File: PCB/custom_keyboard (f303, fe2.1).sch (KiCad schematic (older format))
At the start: 425 parts, among them IC1 FE2.1, J2 Conn_01x03_Male, J5 AVR-ISP-6, Q1 DTC123J, SW1 SW_Push, U1 24LC02BT-I/SN, U10 PRTR5V0U2X, U11 XC6206P332MR, U12 74LVC1G34, U13 XC6206P332MR, U2 PRTR5V0U2X, U3 PRTR5V0U2X, U4 PRTR5V0U2X, U5 PRTR5V0U2X, U6 PRTR5V0U2X, U7 PRTR5V0U2X, U8 PRTR5V0U2X, U9 STM32F303CBT6, Y1 8MHz, Y2 32.768KHz, Y3 12MHz

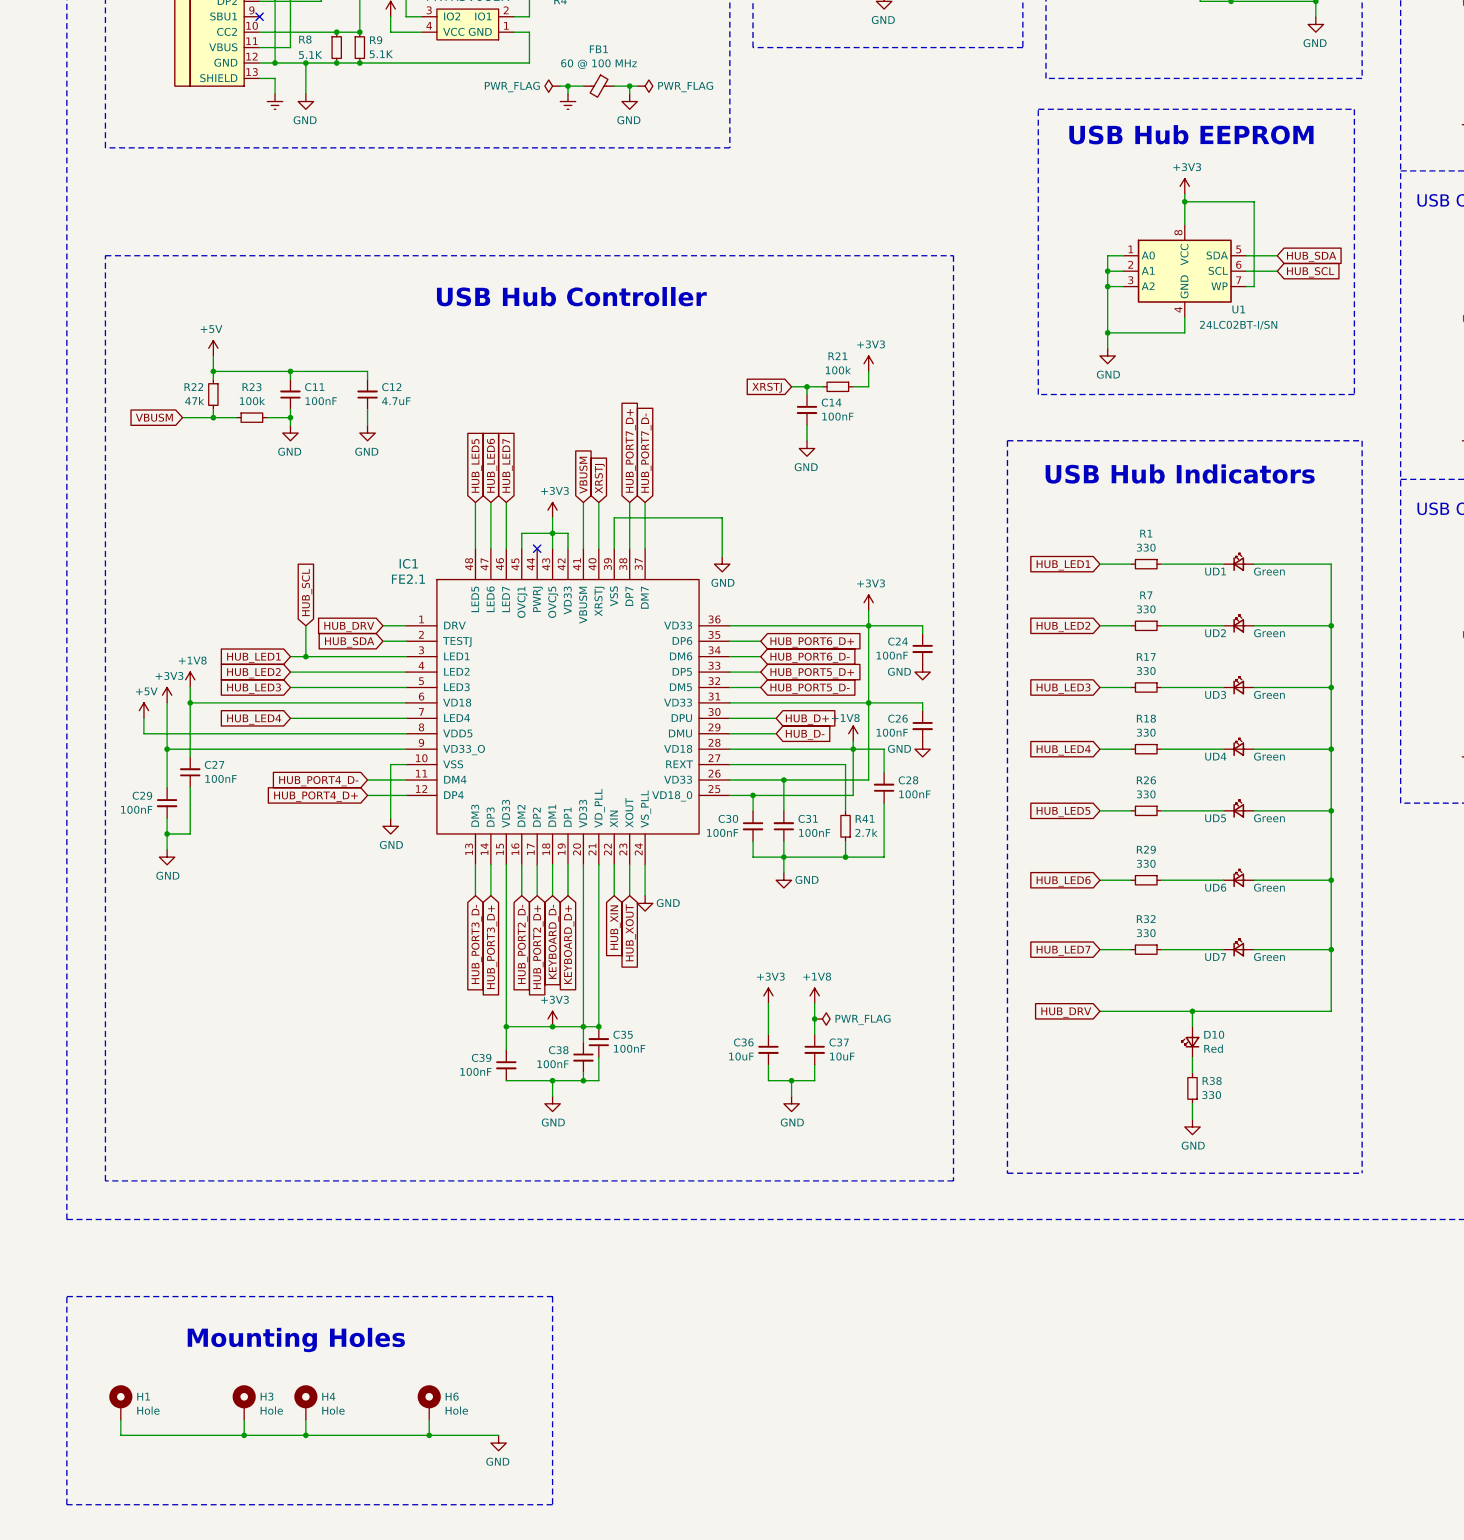
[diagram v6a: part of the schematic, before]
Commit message: Added pullups to EEPROM
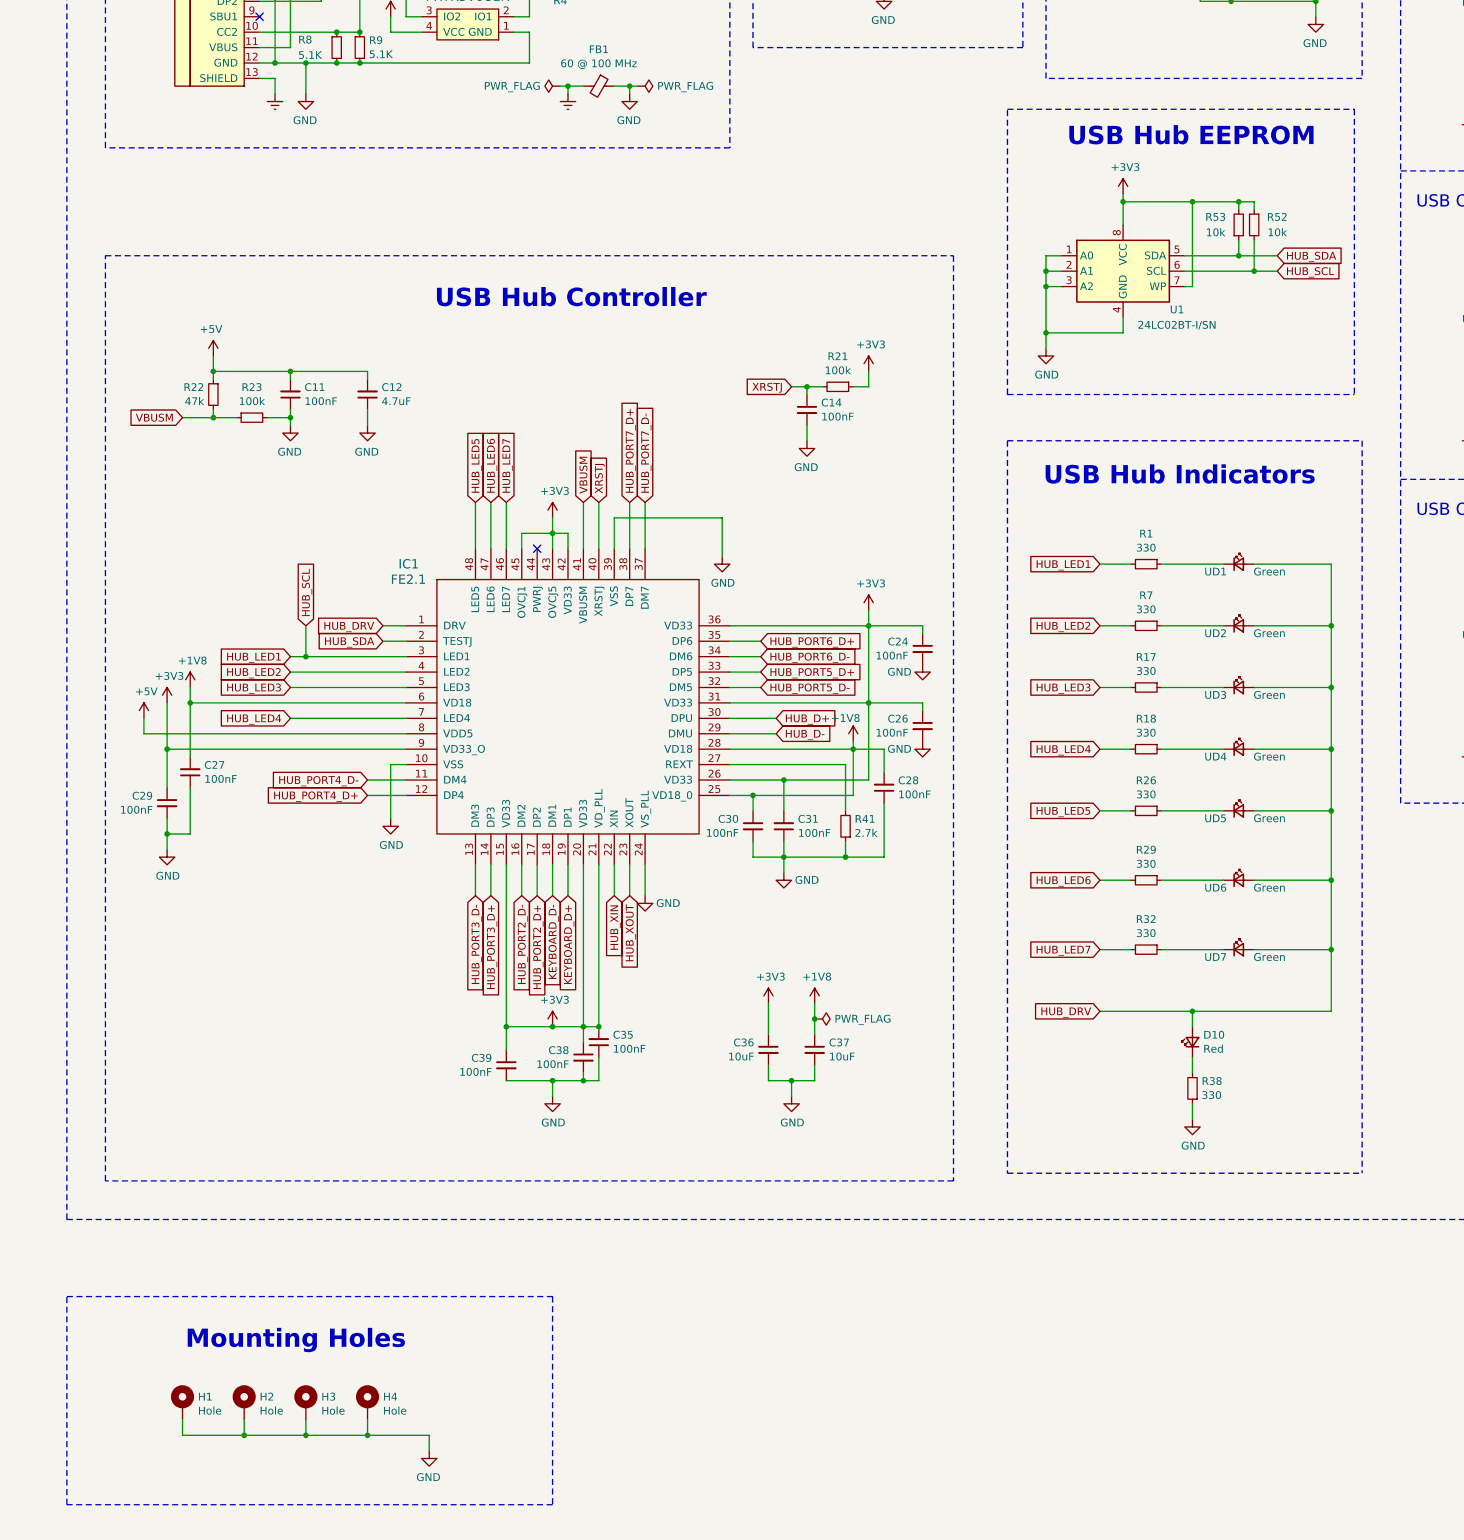
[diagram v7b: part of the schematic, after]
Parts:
- added R52, R53: 10k, Resistor_SMD:R_0805_2012Metric, symbol Device:R_Small
- R50, R51: footprint Resistor_SMD:R_0603_1608Metric -> Resistor_SMD:R_0805_2012Metric
- renumbered H3 to H2, H4 to H3, H6 to H4
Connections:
- net +3V3: now also R52.1, R53.2
- net HUB_LED1: now also R52.2
- net HUB_SDA: now also R53.1
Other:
- moved on the sheet: H1, H4, U1
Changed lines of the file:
@@
 L Memory_EEPROM:24LC02 U1
 U 1 1 AE6F59FC
-P 19850 13900
-F 0 "U1" H 20200 13650 50  0000 C CNN
-F 1 "24LC02BT-I/SN" H 20200 13550 50  0000 C CNN
-F 2 "custom-footprints:24LC04" H 19850 13900 50  0001 C CNN
-F 3 "http://ww1.microchip.com/downloads/en/DeviceDoc/21709c.pdf" H 19850 13900 50  0001 C CNN
-	1    19850 13900
+P 19450 13900
+F 0 "U1" H 19800 13650 50  0000 C CNN
+F 1 "24LC02BT-I/SN" H 19800 13550 50  0000 C CNN
+F 2 "custom-footprints:24LC04" H 19450 13900 50  0001 C CNN
+F 3 "http://ww1.microchip.com/downloads/en/DeviceDoc/21709c.pdf" H 19450 13900 50  0001 C CNN
+	1    19450 13900
 	1    0    0    -1
 $EndComp
@@
 L power:GND #PWR0100
 U 1 1 AE6F9E47
-P 19350 14400
-F 0 "#PWR0100" H 19350 14150 50  0001 C CNN
-F 1 "GND" H 19355 14227 50  0000 C CNN
-F 2 "" H 19350 14400 50  0001 C CNN
-F 3 "" H 19350 14400 50  0001 C CNN
-	1    19350 14400
+P 18950 14400
+F 0 "#PWR0100" H 18950 14150 50  0001 C CNN
+F 1 "GND" H 18955 14227 50  0000 C CNN
+F 2 "" H 18950 14400 50  0001 C CNN
+F 3 "" H 18950 14400 50  0001 C CNN
+	1    18950 14400
 	1    0    0    -1
 $EndComp
 Wire Wire Line
-	19350 14400 19350 14300
+	18950 14400 18950 14300
 Wire Wire Line
-	19350 14300 19850 14300
+	18950 14300 19450 14300
 Wire Wire Line
-	19850 14300 19850 14200
+	19450 14300 19450 14200
 Wire Wire Line
-	19350 14300 19350 14000
+	18950 14300 18950 14000
 Wire Wire Line
-	19350 13800 19450 13800
-Connection ~ 19350 14300
+	18950 13800 19050 13800
+Connection ~ 18950 14300
 Wire Wire Line
-	19450 13900 19350 13900
-Connection ~ 19350 13900
+	19050 13900 18950 13900
+Connection ~ 18950 13900
 Wire Wire Line
-	19350 13900 19350 13800
+	18950 13900 18950 13800
 Wire Wire Line
-	19450 14000 19350 14000
-Connection ~ 19350 14000
+	19050 14000 18950 14000
+Connection ~ 18950 14000
 Wire Wire Line
-	19350 14000 19350 13900
+	18950 14000 18950 13900
 Text GLabel 20450 13900 2    50   Input ~ 0
 HUB_SCL
 Text GLabel 20450 13800 2    50   Input ~ 0
 HUB_SDA
-Wire Wire Line
-	20250 13800 20450 13800
-Wire Wire Line
-	20450 13900 20250 13900
 Text GLabel 16150 17950 3    50   Input ~ 0
 HUB_XIN
@@
 L power:+3V3 #PWR095
 U 1 1 BFCEA814
-P 19850 13400
-F 0 "#PWR095" H 19850 13250 50  0001 C CNN
-F 1 "+3V3" H 19865 13573 50  0000 C CNN
-F 2 "" H 19850 13400 50  0001 C CNN
-F 3 "" H 19850 13400 50  0001 C CNN
-	1    19850 13400
+P 19450 13400
+F 0 "#PWR095" H 19450 13250 50  0001 C CNN
+F 1 "+3V3" H 19465 13573 50  0000 C CNN
+F 2 "" H 19450 13400 50  0001 C CNN
+F 3 "" H 19450 13400 50  0001 C CNN
+	1    19450 13400
 	1    0    0    -1
 $EndComp
 Wire Wire Line
-	19850 13400 19850 13450
+	19450 13400 19450 13450
 Wire Wire Line
-	20250 14000 20300 14000
+	19850 14000 19900 14000
 Wire Wire Line
-	20300 14000 20300 13450
+	19900 14000 19900 13450
 Wire Wire Line
-	20300 13450 19850 13450
-Connection ~ 19850 13450
+	19900 13450 19450 13450
+Connection ~ 19450 13450
 Wire Wire Line
-	19850 13450 19850 13600
+	19450 13450 19450 13600
 Text GLabel 19300 15800 0    50   Input ~ 0
 HUB_LED1
@@
 	20950 12850 20950 14700
 Wire Notes Line
-	20950 14700 18900 14700
-Wire Notes Line
-	18900 12850 20950 12850
-Wire Notes Line
 	18350 13800 18350 19800
 Wire Notes Line
@@
 Wire Wire Line
 	14150 12550 14350 12550
-Wire Notes Line
-	18900 14700 18900 12850
 Connection ~ 23050 16050
 Wire Wire Line
@@
 $EndComp
 $Comp
-L Mechanical:MountingHole_Pad H4
+L Mechanical:MountingHole_Pad H3
 U 1 1 6FB1B5C9
 P 14150 21250
-F 0 "H4" H 14250 21299 50  0000 L CNN
+F 0 "H3" H 14250 21299 50  0000 L CNN
 F 1 "Hole" H 14250 21208 50  0000 L CNN
 F 2 "MountingHole:MountingHole_3.2mm_M3_Pad" H 14150 21250 50  0001 C CNN
@@
 $EndComp
 $Comp
-L Mechanical:MountingHole_Pad H6
+L Mechanical:MountingHole_Pad H4
 U 1 1 6FB1CEC9
-P 14950 21250
-F 0 "H6" H 15050 21299 50  0000 L CNN
-F 1 "Hole" H 15050 21208 50  0000 L CNN
-F 2 "MountingHole:MountingHole_3.2mm_M3_Pad" H 14950 21250 50  0001 C CNN
-F 3 "~" H 14950 21250 50  0001 C CNN
-	1    14950 21250
+P 14550 21250
+F 0 "H4" H 14650 21299 50  0000 L CNN
+F 1 "Hole" H 14650 21208 50  0000 L CNN
+F 2 "MountingHole:MountingHole_3.2mm_M3_Pad" H 14550 21250 50  0001 C CNN
+F 3 "~" H 14550 21250 50  0001 C CNN
+	1    14550 21250
 	1    0    0    -1
 $EndComp
@@
 L power:GND #PWR0283
 U 1 1 7017E3FA
-P 15400 21450
-F 0 "#PWR0283" H 15400 21200 50  0001 C CNN
-F 1 "GND" H 15405 21277 50  0000 C CNN
-F 2 "" H 15400 21450 50  0001 C CNN
-F 3 "" H 15400 21450 50  0001 C CNN
-	1    15400 21450
+P 14950 21550
+F 0 "#PWR0283" H 14950 21300 50  0001 C CNN
+F 1 "GND" H 14955 21377 50  0000 C CNN
+F 2 "" H 14950 21550 50  0001 C CNN
+F 3 "" H 14950 21550 50  0001 C CNN
+	1    14950 21550
 	-1   0    0    -1
 $EndComp
 Wire Wire Line
-	15400 21450 14950 21450
-Wire Wire Line
 	14150 21450 14150 21350
 Wire Wire Line
-	14950 21350 14950 21450
+	14550 21350 14550 21450
 $Comp
 L Mechanical:MountingHole_Pad H1
 U 1 1 72E52B19
-P 12950 21250
-F 0 "H1" H 13050 21299 50  0000 L CNN
-F 1 "Hole" H 13050 21208 50  0000 L CNN
-F 2 "MountingHole:MountingHole_3.2mm_M3_Pad" H 12950 21250 50  0001 C CNN
-F 3 "~" H 12950 21250 50  0001 C CNN
-	1    12950 21250
+P 13350 21250
+F 0 "H1" H 13450 21299 50  0000 L CNN
+F 1 "Hole" H 13450 21208 50  0000 L CNN
+F 2 "MountingHole:MountingHole_3.2mm_M3_Pad" H 13350 21250 50  0001 C CNN
+F 3 "~" H 13350 21250 50  0001 C CNN
+	1    13350 21250
 	1    0    0    -1
 $EndComp
 $Comp
-L Mechanical:MountingHole_Pad H3
+L Mechanical:MountingHole_Pad H2
 U 1 1 72E561B5
 P 13750 21250
-F 0 "H3" H 13850 21299 50  0000 L CNN
+F 0 "H2" H 13850 21299 50  0000 L CNN
 F 1 "Hole" H 13850 21208 50  0000 L CNN
 F 2 "MountingHole:MountingHole_3.2mm_M3_Pad" H 13750 21250 50  0001 C CNN
@@
 $EndComp
 Wire Wire Line
-	12950 21450 12950 21350
+	13350 21450 13350 21350
 Wire Wire Line
 	13750 21350 13750 21450
-Connection ~ 14950 21450
 Connection ~ 13750 21450
 Wire Wire Line
@@
 KEYBOARD_D+
 Wire Wire Line
-	12950 21450 13750 21450
-Wire Wire Line
-	14150 21450 14950 21450
+	14150 21450 14550 21450
 $Comp
 L power:+5V #PWR0158
@@
 F 0 "R51" V 9700 20500 50  0000 C CNN
 F 1 "10k" V 9600 20500 50  0000 C CNN
-F 2 "Resistor_SMD:R_0603_1608Metric" H 9800 20500 50  0001 C CNN
+F 2 "Resistor_SMD:R_0805_2012Metric" H 9800 20500 50  0001 C CNN
 F 3 "~" H 9800 20500 50  0001 C CNN
 	1    9800 20500
@@
 F 0 "R50" V 9600 20350 50  0000 C CNN
 F 1 "10k" V 9700 20350 50  0000 C CNN
-F 2 "Resistor_SMD:R_0603_1608Metric" H 9800 20350 50  0001 C CNN
+F 2 "Resistor_SMD:R_0805_2012Metric" H 9800 20350 50  0001 C CNN
 F 3 "~" H 9800 20350 50  0001 C CNN
 	1    9800 20350
 	0    -1   1    0
 $EndComp
+$Comp
+L Device:R_Small R53
+U 1 1 61D98DD0
+P 20200 13600
+F 0 "R53" H 20050 13550 50  0000 C CNN
+F 1 "10k" H 20050 13650 50  0000 C CNN
+F 2 "Resistor_SMD:R_0805_2012Metric" H 20200 13600 50  0001 C CNN
+F 3 "~" H 20200 13600 50  0001 C CNN
+	1    20200 13600
+	1    0    0    1
+$EndComp
+Wire Notes Line
+	18700 14700 18700 12850
+Wire Notes Line
+	18700 12850 20950 12850
+Wire Notes Line
+	18700 14700 20950 14700
+Wire Wire Line
+	13350 21450 13750 21450
+Wire Wire Line
+	14550 21450 14950 21450
+Wire Wire Line
+	14950 21450 14950 21550
+Connection ~ 14550 21450
+Wire Wire Line
+	19850 13800 20200 13800
+Connection ~ 20200 13800
+Wire Wire Line
+	20200 13800 20450 13800
+Wire Wire Line
+	19850 13900 20300 13900
+Connection ~ 20300 13900
+Wire Wire Line
+	20300 13900 20450 13900
+Wire Wire Line
+	20200 13700 20200 13800
+Wire Wire Line
+	20300 13700 20300 13900
+$Comp
+L Device:R_Small R52
+U 1 1 61D9C5AC
+P 20300 13600
+F 0 "R52" H 20150 13650 50  0000 C CNN
+F 1 "10k" H 20150 13550 50  0000 C CNN
+F 2 "Resistor_SMD:R_0805_2012Metric" H 20300 13600 50  0001 C CNN
+F 3 "~" H 20300 13600 50  0001 C CNN
+	1    20300 13600
+	-1   0    0    -1
+$EndComp
+Wire Wire Line
+	20300 13500 20300 13450
+Wire Wire Line
+	20300 13450 20200 13450
+Connection ~ 19900 13450
+Wire Wire Line
+	20200 13500 20200 13450
+Connection ~ 20200 13450
+Wire Wire Line
+	20200 13450 19900 13450
 $EndSCHEMATC

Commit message: Added power control to downstream ports
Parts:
- added C44, C46: 10uF, Capacitor_SMD:C_0805_2012Metric, symbol Device:C_Small
- added C45, C47: 0.1uF, Capacitor_SMD:C_0805_2012Metric, symbol Device:C_Small
- added R54, R55, R56: 100k, Resistor_SMD:R_0603_1608Metric, symbol Device:R_Small
- added TP1: HUB_D-, symbol Connector:TestPoint
- added TP2: HUB_D+, symbol Connector:TestPoint
- added TP3: INPUT_GND, symbol Connector:TestPoint
- added TP4: EXTRA_1, symbol Connector:TestPoint
- added U14, U15: MIC2505, custom-footprints:MIC2505, symbol custom:MIC2505
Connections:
- net +3V3: now also R54.1, R55.1, R56.1; no longer IC1.43 (OVCJ5), IC1.45 (OVCJ1)
- net +5V: now also C45.1, C47.1, U14.5 (IN), U14.7 (IN), U15.5 (IN), U15.7 (IN); no longer C10.1, C13.1, C2.1, C23.1, C25.1, C34.1, C40.1, F2.1, F2.2, F3.1, F3.2, F4.1, F4.2, F5.1, F5.2, F6.1, F6.2, F7.1, F7.2, U11.3 (VI), USB2.11 (VBUS), USB2.2 (VBUS), USB3.1 (VBUS), USB4.1 (VBUS), USB5.11 (VBUS), USB5.2 (VBUS), USB6.1 (VBUS), USB7.11 (VBUS), USB7.2 (VBUS)
- net EXTRA_1: now also TP4.1
- net GND: now also C44.2, C45.2, C46.2, C47.2, TP3.1, U14.3 (GND), U15.3 (GND)
- net HUB_D+: now also TP2.1
- net HUB_D-: now also TP1.1
- net KEYBOARD_SCL: now also OL1.2 (SCL), R51.2; no longer OL1.1 (SDA), R50.1
- net KEYBOARD_SDA: now also OL1.1 (SDA), R50.1; no longer OL1.2 (SCL), R51.2
- net PWRJ: now reaches IC1.44 (PWRJ)
- net PWRJ: now also R55.2, U14.1 (CTL), U15.1 (CTL)
- new net: C44.1, U14.4 (GATE)
- new net: C46.1, U15.4 (GATE)
- new net OVCJ1: IC1.45 (OVCJ1), R54.2, U14.2 (FLG)
- new net OVCJ5: IC1.43 (OVCJ5), R56.2, U15.2 (FLG)
- new net PORT1-4_PWR: C23.1, C25.1, C34.1, C40.1, F5.1, F5.2, F6.1, F6.2, F7.1, F7.2, U11.3 (VI), U14.6 (OUT), U14.8 (OUT), USB2.11 (VBUS), USB2.2 (VBUS), USB3.1 (VBUS), USB4.1 (VBUS)
- new net PORT5-7PWR: C10.1, C13.1, C2.1, F2.1, F2.2, F3.1, F3.2, F4.1, F4.2, U15.6 (OUT), U15.8 (OUT), USB5.11 (VBUS), USB5.2 (VBUS), USB6.1 (VBUS), USB7.11 (VBUS), USB7.2 (VBUS)
- no-connect marks 10 -> 9
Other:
- note added: "USB Downstream Power\n"
- moved on the sheet: C23, C40, C41, F2, F3, F4, F6, F7, FB5, R31, R33, R35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
